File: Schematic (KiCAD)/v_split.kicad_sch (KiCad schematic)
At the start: 80 parts, among them P6 Reg 2 DFF-Reset N, T1 INVERT, T10 INVERT, T12 T-FF Preload, T13 INVERT, T14 INVERT, T15 T-FF Preload, T16 INVERT, T17 INVERT, T18 T-FF Preload, T19 INVERT, T2 INVERT, T20 INVERT, T21 T-FF Preload, T22 INVERT, T23 INVERT, T24 T-FF Preload, T25 INVERT, T26 INVERT, T27 T-FF Preload, T28 INVERT, T29 INVERT, T3 NAND_2, T30 T-FF Preload, T31 INVERT, T4 D-FF-SR, T6 INVERT, T7 INVERT, T8 T-FF Preload, T9 INVERT

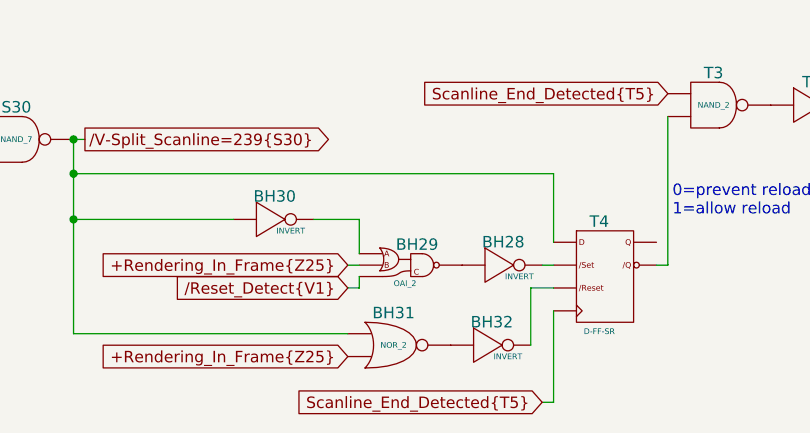
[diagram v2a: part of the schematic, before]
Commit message: - Updated all of the various And-OR-Invert gates to have consistent names.  - Added the schematic for CL3 / SL3 GPIO pins.  There are no surprises revealed by this.  - Finished up the CPU address decoding tracing.  - Added one of the 'artifact' counters from the pulse channels
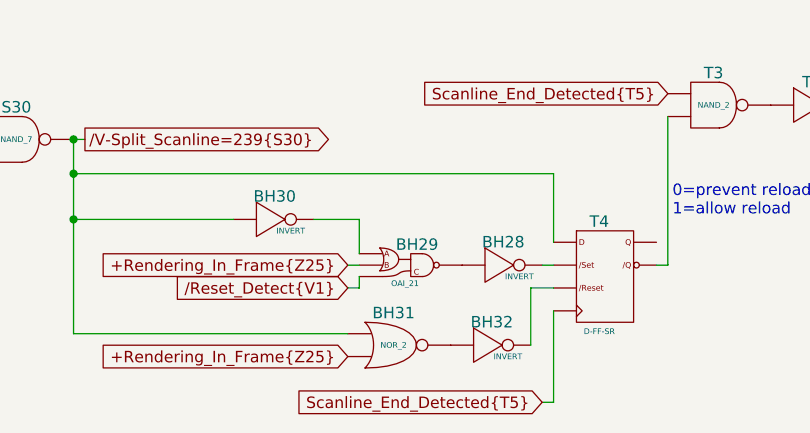
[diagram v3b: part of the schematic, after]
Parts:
- BH29: value OAI_2 -> OAI_21
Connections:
- net at V4. (X): now also V5. (X); no longer V6. (X)
- net at V9. (X): now also V11. (X); no longer V4. (X)
- net at BH28. (X): now also BH29. (X); no longer T4. (/Q)
- net at BH32. (X): now also BH31. (X); no longer T4. (/Q)
- net at T2. (X): now also T1. (X); no longer T3. (X)
- net at T20. (X): now also T21. (/Q); no longer V27. (X)
- net at T21. (/Q): now also V28. (X), V29. (X); no longer T20. (X)
- net at T14. (X): now also T15. (/Q); no longer V19. (X)
- net at V7. (X): now also N4. (X); no longer V8. (/Q)
- net at N4. (X): now also N3. (X); no longer V7. (X)
- net at T29. (X): now also V36. (X); no longer T30. (/Q)
- net at V11. (X): now also V10. (X); no longer V12. (X)
- net at T26. (X): now also T27. (/Q); no longer V33. (X)
- net at T27. (/Q): no longer T26. (X)
- net at T12. (/Q): now also T8. (/Q), T9. (X)
- net at T10. (X): now also V16. (X); no longer T12. (/Q)
- net at T30. (/Q): now also V37. (X), V38. (X); no longer T31. (X)
- net at T23. (X): now also V30. (X); no longer T24. (/Q)
- net at T15. (/Q): no longer T14. (X)
- net at T7. (X): now also T8. (/Q); no longer V13. (X)
- net at T18. (/Q): now also T17. (X)
- net at T17. (X): now also V22. (X); no longer T18. (/Q)
- new net: N1. (X), P6. (/Q1)
- new net: V4. (X), V6. (X)
- new net: V3. (X), V4. (X)
- new net: V4. (X), V9. (X)
- new net: T3. (X), T4. (/Q)
- new net: BH28. (X), T4. (/Q)
- new net: BH32. (X), T4. (/Q)
- new net: T2. (X), T3. (X)
- new net: T18. (/Q), T19. (X), T21. (/Q)
- new net: T15. (/Q), T16. (X), T18. (/Q)
- new net: V6. (X), W2. (Q4)
- new net: T20. (X), V27. (X)
- new net: T27. (/Q), V34. (X), V35. (X)
- new net: V33. (X), V34. (X)
- new net: V19. (X), V20. (X)
- new net: T14. (X), V19. (X)
- new net: V7. (X), V8. (/Q)
- new net: V27. (X), V28. (X)
- new net: V3. (X), W2. (Q4)
- new net: T29. (X), T30. (/Q)
- new net: T18. (/Q), V23. (X), V26. (X)
- new net: V26. (X), W3,V24,V25,V41. (Q7)
- new net: V8. (/Q), V9. (X)
- new net: N3. (X), N4. (X), N5. (X)
- new net: V35. (X), W3,V24,V25,V41. (Q7)
- new net: V11. (X), V12. (X)
- new net: V12. (X), W2. (Q4)
- new net: T24. (/Q), T25. (X), T27. (/Q)
- new net: T26. (X), V33. (X)
- new net: T15. (/Q), V20. (X), V21. (X)
- new net: R4. (Q1), S4. (X)
- new net: R4. (Q1), S3. (X)
- new net: T12. (/Q), V17. (X), V18. (X)
- new net: T12. (/Q), T13. (X), T15. (/Q)
- new net: T10. (X), T12. (/Q)
- new net: V22. (X), V23. (X)
- new net: V18. (X), W3,V24,V25,V41. (Q7)
- new net: T30. (/Q), T31. (X)
- new net: T23. (X), T24. (/Q)
- new net: T21. (/Q), T22. (X), T24. (/Q)
- new net: BH29. (X), BH30. (X)
- new net: T27. (/Q), T28. (X), T30. (/Q)
- new net: V16. (X), V17. (X)
- new net: T7. (X), V13. (X)
- new net: V13. (X), V14. (X)
- new net: V5. (X), W2. (Q4)
- new net: V36. (X), V37. (X)
- new net: T24. (/Q), V31. (X), V32. (X)
- new net: V32. (X), W3,V24,V25,V41. (Q7)
- new net: V29. (X), W3,V24,V25,V41. (Q7)
- new net: T6. (X), V11. (X)
- new net: V30. (X), V31. (X)
- new net: V38. (X), W3,V24,V25,V41. (Q7)
- new net: T8. (/Q), V14. (X), V15. (X)
- new net: V2. (X), W2. (Q4)
- new net: V21. (X), W3,V24,V25,V41. (Q7)
- new net: V15. (X), W3,V24,V25,V41. (Q7)
- new net: V10. (X), W2. (Q4)
- now unconnected: T15. (/Q), T15. (/Q), T15. (/Q), T24. (/Q), T24. (/Q), T24. (/Q), T27. (/Q), T27. (/Q), T27. (/Q)
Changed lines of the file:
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@@
 	)
 	(symbol
-		(lib_name "Reg_2_DFF-Reset_N_1")
 		(lib_id "MMC5:Reg_2_DFF-Reset_N")
 		(at 250.19 111.76 0)
@@
 	)
 	(symbol
-		(lib_name "NAND_2_7")
 		(lib_id "MMC5:NAND_2")
 		(at 344.17 191.77 0)
@@
 	)
 	(symbol
-		(lib_name "INVERT_21")
 		(lib_id "MMC5:INVERT")
 		(at 158.75 82.55 0)
@@
 	)
 	(symbol
-		(lib_name "INVERT_6")
+		(lib_name "INVERT_1")
 		(lib_id "MMC5:INVERT")
 		(at 158.75 66.04 0)
@@
 	)
 	(symbol
-		(lib_name "XNOR_2_2")
 		(lib_id "MMC5:XNOR_2")
 		(at 306.07 87.63 0)
@@
 	)
 	(symbol
-		(lib_name "INVERT_22")
+		(lib_name "INVERT_4")
 		(lib_id "MMC5:INVERT")
 		(at 133.35 102.87 0)
@@
 	)
 	(symbol
-		(lib_name "NAND_2_25")
+		(lib_name "NAND_2_3")
 		(lib_id "MMC5:NAND_2")
 		(at 110.49 134.62 0)
@@
 	)
 	(symbol
-		(lib_name "NAND_2_12")
+		(lib_name "NAND_2_1")
 		(lib_id "MMC5:NAND_2")
 		(at 121.92 69.85 0)
@@
 	)
 	(symbol
-		(lib_name "INVERT_8")
+		(lib_name "INVERT_10")
 		(lib_id "MMC5:INVERT")
 		(at 351.79 101.6 0)
@@
 	)
 	(symbol
-		(lib_name "NAND_2_18")
+		(lib_name "NAND_2_9")
 		(lib_id "MMC5:NAND_2")
 		(at 121.92 102.87 0)
@@
 	)
 	(symbol
+		(lib_name "XNOR_2_1")
 		(lib_id "MMC5:XNOR_2")
 		(at 306.07 72.39 0)
@@
 	)
 	(symbol
-		(lib_name "INVERT_28")
+		(lib_name "INVERT_7")
 		(lib_id "MMC5:INVERT")
 		(at 133.35 152.4 0)
@@
 	)
 	(symbol
-		(lib_name "INVERT_9")
+		(lib_name "INVERT_14")
 		(lib_id "MMC5:INVERT")
 		(at 364.49 191.77 0)
@@
 	)
 	(symbol
-		(lib_name "NAND_2_14")
+		(lib_name "NAND_2_7")
 		(lib_id "MMC5:NAND_2")
 		(at 99.06 81.28 0)
@@
 	)
 	(symbol
-		(lib_name "NAND_2_23")
+		(lib_name "NAND_2_2")
 		(lib_id "MMC5:NAND_2")
 		(at 99.06 130.81 0)
@@
 	)
 	(symbol
-		(lib_name "INVERT_17")
+		(lib_name "INVERT_12")
 		(lib_id "MMC5:INVERT")
 		(at 321.31 209.55 0)
@@
 	)
 	(symbol
-		(lib_name "XNOR_2_4")
+		(lib_name "XNOR_2_2")
 		(lib_id "MMC5:XNOR_2")
 		(at 306.07 102.87 0)
@@
 	)
 	(symbol
-		(lib_name "INVERT_25")
+		(lib_name "INVERT_15")
 		(lib_id "MMC5:INVERT")
 		(at 158.75 115.57 0)
@@
 	)
 	(symbol
-		(lib_name "INVERT_26")
+		(lib_name "INVERT_13")
 		(lib_id "MMC5:INVERT")
 		(at 133.35 135.89 0)
@@
 	)
 	(symbol
-		(lib_name "NAND_2_13")
+		(lib_name "NAND_2_5")
 		(lib_id "MMC5:NAND_2")
 		(at 110.49 68.58 0)
@@
 	)
 	(symbol
-		(lib_name "NAND_2_16")
+		(lib_name "NAND_2_6")
 		(lib_id "MMC5:NAND_2")
 		(at 110.49 85.09 0)
@@
 	)
 	(symbol
-		(lib_name "NAND_2_1")
+		(lib_name "NAND_2_8")
 		(lib_id "MMC5:NAND_2")
 		(at 99.06 48.26 0)
@@
 	)
 	(symbol
-		(lib_name "NOR_2_2")
 		(lib_id "MMC5:NOR_2")
 		(at 328.93 101.6 0)
@@
 	)
 	(symbol
-		(lib_name "INVERT_3")
+		(lib_name "INVERT_5")
 		(lib_id "MMC5:INVERT")
 		(at 158.75 49.53 0)
@@
 	)
 	(symbol
-		(lib_name "INVERT_29")
+		(lib_name "INVERT_3")
 		(lib_id "MMC5:INVERT")
 		(at 158.75 148.59 0)
@@
 	)
 	(symbol
-		(lib_name "INVERT_10")
+		(lib_name "INVERT_8")
 		(lib_id "MMC5:INVERT")
 		(at 355.6 191.77 0)
@@
 	)
 	(symbol
-		(lib_name "INVERT_24")
+		(lib_name "INVERT_2")
 		(lib_id "MMC5:INVERT")
 		(at 133.35 119.38 0)
@@
 	)
 	(symbol
-		(lib_name "INVERT_2")
+		(lib_name "INVERT_6")
 		(lib_id "MMC5:INVERT")
 		(at 133.35 53.34 0)
@@
 	)
 	(symbol
-		(lib_name "INVERT_5")
+		(lib_name "INVERT_11")
 		(lib_id "MMC5:INVERT")
 		(at 133.35 69.85 0)
@@
 	)
 	(symbol
-		(lib_name "T-FF_Preload_4")
+		(lib_name "T-FF_Preload_2")
 		(lib_id "MMC5:T-FF_Preload")
 		(at 147.32 97.79 0)
@@
 			)
 		)
-		(property "Value" "OAI_2"
+		(property "Value" "OAI_21"
 			(at 309.88 211.582 0)
 			(do_not_autoplace yes)
@@
 	)
 	(symbol
-		(lib_name "NAND_2_24")
+		(lib_name "NAND_2_4")
 		(lib_id "MMC5:NAND_2")
 		(at 121.92 135.89 0)
@@
 	)
 	(symbol
-		(lib_name "INVERT_23")
+		(lib_name "INVERT_9")
 		(lib_id "MMC5:INVERT")
 		(at 158.75 99.06 0)
@@
 	)
 	(symbol
-		(lib_name "T-FF_Preload_7")
 		(lib_id "MMC5:T-FF_Preload")
 		(at 147.32 147.32 0)
@@
 	)
 	(symbol
-		(lib_name "NAND_2_10")
+		(lib_name "NAND_2_11")
 		(lib_id "MMC5:NAND_2")
 		(at 121.92 53.34 0)
@@
 	)
 	(symbol
-		(lib_name "T-FF_Preload_6")
+		(lib_name "T-FF_Preload_3")
 		(lib_id "MMC5:T-FF_Preload")
 		(at 147.32 130.81 0)
@@
 	)
 	(symbol
-		(lib_name "NAND_2_5")
+		(lib_name "NAND_2_10")
 		(lib_id "MMC5:NAND_2")
 		(at 121.92 36.83 0)
@@
 	)
 	(symbol
-		(lib_name "XNOR_2_1")
+		(lib_name "XNOR_2_3")
 		(lib_id "MMC5:XNOR_2")
 		(at 306.07 80.01 0)
@@
 	)
 	(symbol
-		(lib_name "NAND_2_28")
+		(lib_name "NAND_2_12")
 		(lib_id "MMC5:NAND_2")
 		(at 110.49 151.13 0)
@@
 	)
 	(symbol
-		(lib_name "NAND_2_20")
+		(lib_name "NAND_2_14")
 		(lib_id "MMC5:NAND_2")
 		(at 99.06 114.3 0)
@@
 	)
 	(symbol
-		(lib_name "NAND_2_17")
+		(lib_name "NAND_2_13")
 		(lib_id "MMC5:NAND_2")
 		(at 99.06 97.79 0)
@@
 	)
 	(symbol
-		(lib_name "NAND_2_27")
+		(lib_name "NAND_2_15")
 		(lib_id "MMC5:NAND_2")
 		(at 121.92 152.4 0)
@@
 	)
 	(symbol
-		(lib_name "T-FF_Preload_5")
+		(lib_name "T-FF_Preload_4")
 		(lib_id "MMC5:T-FF_Preload")
 		(at 147.32 114.3 0)
@@
 	)
 	(symbol
-		(lib_name "INVERT_4")
+		(lib_name "INVERT_16")
 		(lib_id "MMC5:INVERT")
 		(at 158.75 33.02 0)
@@
 	)
 	(symbol
-		(lib_name "T-FF_Preload_2")
+		(lib_name "T-FF_Preload_5")
 		(lib_id "MMC5:T-FF_Preload")
 		(at 147.32 64.77 0)
@@
 	)
 	(symbol
-		(lib_name "INVERT_19")
+		(lib_name "INVERT_17")
 		(lib_id "MMC5:INVERT")
 		(at 320.04 218.44 0)
@@
 	)
 	(symbol
-		(lib_name "NAND_2_19")
+		(lib_name "NAND_2_22")
 		(lib_id "MMC5:NAND_2")
 		(at 110.49 101.6 0)
@@
 	)
 	(symbol
-		(lib_name "INVERT_1")
+		(lib_name "INVERT_22")
 		(lib_id "MMC5:INVERT")
 		(at 133.35 36.83 0)
@@
 	)
 	(symbol
-		(lib_name "T-FF_Preload_3")
+		(lib_name "T-FF_Preload_6")
 		(lib_id "MMC5:T-FF_Preload")
 		(at 147.32 81.28 0)
@@
 	)
 	(symbol
-		(lib_name "NAND_2_22")
+		(lib_name "NAND_2_19")
 		(lib_id "MMC5:NAND_2")
 		(at 110.49 118.11 0)
@@
 	)
 	(symbol
-		(lib_name "INVERT_7")
+		(lib_name "INVERT_18")
 		(lib_id "MMC5:INVERT")
 		(at 308.61 110.49 0)
@@
 	)
 	(symbol
-		(lib_name "NAND_2_31")
+		(lib_name "NAND_2_25")
 		(lib_id "MMC5:NAND_2")
 		(at 364.49 91.44 0)
@@
 	)
 	(symbol
-		(lib_name "NAND_2_26")
+		(lib_name "NAND_2_16")
 		(lib_id "MMC5:NAND_2")
 		(at 99.06 147.32 0)
@@
 	)
 	(symbol
-		(lib_name "INVERT_18")
+		(lib_name "INVERT_19")
 		(lib_id "MMC5:INVERT")
 		(at 295.91 204.47 0)
@@
 	)
 	(symbol
-		(lib_name "NAND_2_15")
+		(lib_name "NAND_2_24")
 		(lib_id "MMC5:NAND_2")
 		(at 121.92 86.36 0)
@@
 	)
 	(symbol
-		(lib_name "NAND_2_6")
+		(lib_name "NAND_2_20")
 		(lib_id "MMC5:NAND_2")
 		(at 110.49 35.56 0)
@@
 	)
 	(symbol
-		(lib_name "BUFFER_5")
 		(lib_id "MMC5:BUFFER")
 		(at 238.76 99.06 0)
@@
 	)
 	(symbol
-		(lib_name "INVERT_27")
+		(lib_name "INVERT_21")
 		(lib_id "MMC5:INVERT")
 		(at 158.75 132.08 0)
@@
 	)
 	(symbol
-		(lib_name "NAND_2_2")
+		(lib_name "NAND_2_17")
 		(lib_id "MMC5:NAND_2")
 		(at 99.06 64.77 0)
@@
 	)
 	(symbol
-		(lib_name "NAND_2_21")
+		(lib_name "NAND_2_23")
 		(lib_id "MMC5:NAND_2")
 		(at 121.92 119.38 0)
@@
 	)
 	(symbol
-		(lib_name "NAND_2_11")
+		(lib_name "NAND_2_21")
 		(lib_id "MMC5:NAND_2")
 		(at 110.49 52.07 0)
@@
 	)
 	(symbol
-		(lib_name "XNOR_2_3")
+		(lib_name "XNOR_2_4")
 		(lib_id "MMC5:XNOR_2")
 		(at 306.07 95.25 0)
@@
 	)
 	(symbol
-		(lib_name "BUFFER_4")
+		(lib_name "BUFFER_1")
 		(lib_id "MMC5:BUFFER")
 		(at 238.76 124.46 0)
@@
 	)
 	(symbol
+		(lib_name "NAND_2_18")
 		(lib_id "MMC5:NAND_2")
 		(at 99.06 31.75 0)
@@
 	)
 	(symbol
-		(lib_name "NAND_2_9")
+		(lib_name "NAND_2_26")
 		(lib_id "MMC5:NAND_2")
 		(at 375.92 92.71 0)
@@
 	)
 	(symbol
+		(lib_name "T-FF_Preload_7")
 		(lib_id "MMC5:T-FF_Preload")
 		(at 147.32 31.75 0)
